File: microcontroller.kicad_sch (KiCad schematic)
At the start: 13 parts, among them SW1 Boot Switch, SW2 System Reset, U2 STM32F401RETx

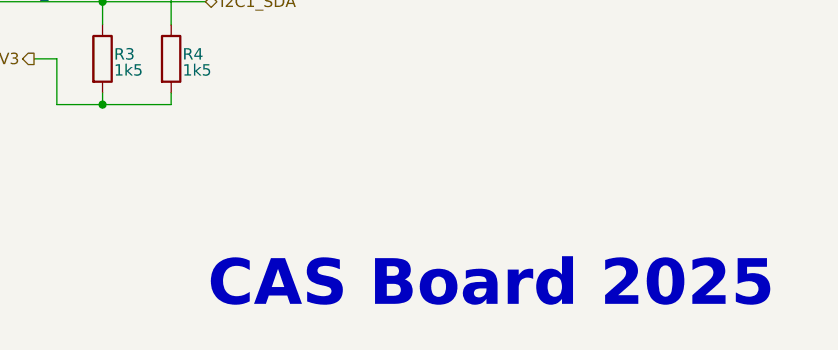
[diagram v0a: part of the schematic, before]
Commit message: remove camera power and interface headers and pins from schematic and PCB
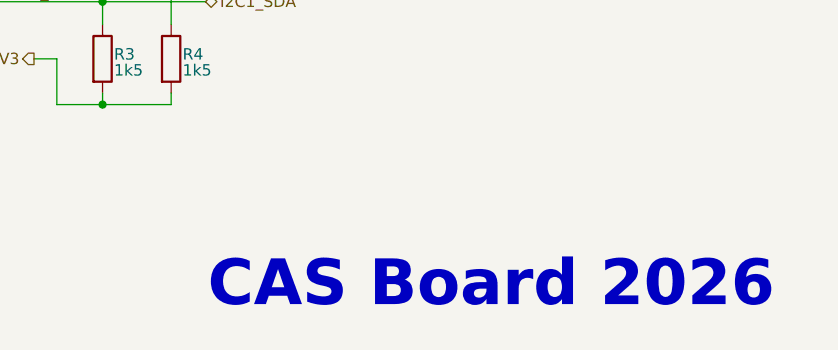
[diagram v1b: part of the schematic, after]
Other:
- note added: "CAS Board 2026"
- note removed: "CAS Board 2025"
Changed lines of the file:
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@@
 		)
 	)
-	(text "CAS Board 2025\n\n"
+	(text "CAS Board 2026"
 		(exclude_from_sim no)
-		(at 209.55 177.8 0)
+		(at 209.55 173.736 0)
 		(effects
 			(font
